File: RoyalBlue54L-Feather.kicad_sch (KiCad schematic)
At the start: 6 parts

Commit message: Renamed to RoyalBlue54L-Feather
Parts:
- U7: footprint RoyalBlue-nRF54L15-Symbol:RoyalBlue54L_QRCode -> RoyalBlue54L-Feather-Symbol:RoyalBlue54L_QRCode
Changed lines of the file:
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@@
 			)
 		)
-		(property "Footprint" "RoyalBlue-nRF54L15-Symbol:RoyalBlue54L_QRCode"
+		(property "Footprint" "RoyalBlue54L-Feather-Symbol:RoyalBlue54L_QRCode"
 			(at 271.78 137.16 0)
 			(effects
@@
 		)
 		(instances
-			(project "RoyalBlue-nRF54L15"
+			(project "RoyalBlue54L-Feather"
 				(path "/ba76ff89-c129-45ae-a3c9-97538370856c"
 					(reference "LOGO1")
@@
 		)
 		(instances
-			(project "RoyalBlue-nRF54L15"
+			(project "RoyalBlue54L-Feather"
 				(path "/ba76ff89-c129-45ae-a3c9-97538370856c"
 					(page "5")
@@
 		)
 		(instances
-			(project "RoyalBlue-nRF54L15"
+			(project "RoyalBlue54L-Feather"
 				(path "/ba76ff89-c129-45ae-a3c9-97538370856c"
 					(page "3")
@@
 		)
 		(instances
-			(project "RoyalBlue-nRF54L15"
+			(project "RoyalBlue54L-Feather"
 				(path "/ba76ff89-c129-45ae-a3c9-97538370856c"
 					(page "4")
@@
 		)
 		(instances
-			(project "RoyalBlue-nRF54L15"
+			(project "RoyalBlue54L-Feather"
 				(path "/ba76ff89-c129-45ae-a3c9-97538370856c"
 					(page "2")

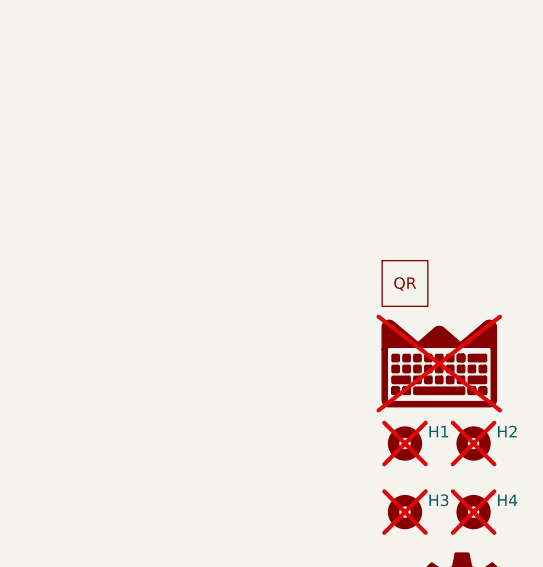
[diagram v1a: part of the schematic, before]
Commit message: Added testpoints, moved USB connection to VSYS.
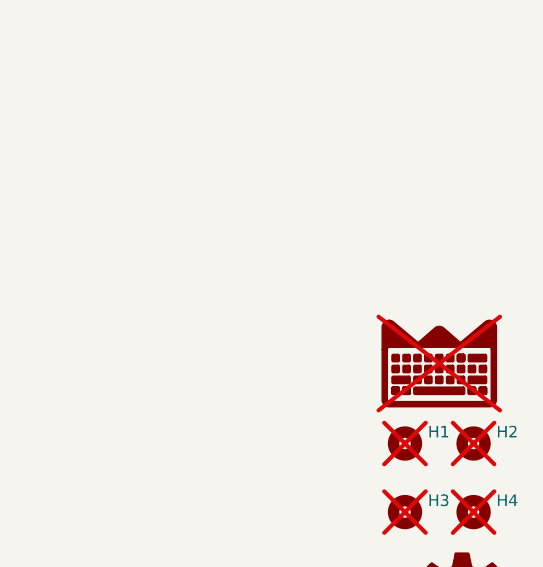
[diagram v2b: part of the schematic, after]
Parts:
- removed U7: ~, RoyalBlue54L-Feather-Symbol:RoyalBlue54L_QRCode, symbol LordsBoards-Graphic:QRCode
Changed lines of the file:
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@@
-	)
-	(symbol
-		(lib_id "LordsBoards-Graphic:QRCode")
-		(at 271.78 137.16 0)
-		(unit 1)
-		(exclude_from_sim yes)
-		(in_bom no)
-		(on_board yes)
-		(dnp no)
-		(fields_autoplaced yes)
-		(property "Reference" "U7"
-			(at 271.78 137.16 0)
-			(effects
-				(font
-					(size 1.27 1.27)
-				)
-				(hide yes)
-			)
-		)
-		(property "Value" "~"
-			(at 271.78 137.16 0)
-			(effects
-				(font
-					(size 1.27 1.27)
-				)
-				(hide yes)
-			)
-		)
-		(property "Footprint" "RoyalBlue54L-Feather-Symbol:RoyalBlue54L_QRCode"
-			(at 271.78 137.16 0)
-			(effects
-				(font
-					(size 1.27 1.27)
-				)
-				(hide yes)
-			)
-		)
-		(property "Datasheet" ""
-			(at 271.78 137.16 0)
-			(effects
-				(font
-					(size 1.27 1.27)
-				)
-				(hide yes)
-			)
-		)
-		(property "Description" ""
-			(at 271.78 137.16 0)
-			(effects
-				(font
-					(size 1.27 1.27)
-				)
-				(hide yes)
-			)
-		)
-		(instances
-			(project ""
-				(path "/ba76ff89-c129-45ae-a3c9-97538370856c"
-					(reference "U7")
-					(unit 1)
-				)
-			)
-		)
 	)
 	(symbol
